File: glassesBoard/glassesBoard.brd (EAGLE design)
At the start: 87.4 x 30.9 mm, 131 parts, among them J1 BM10NB(0.8)-16DS-0.4V(51), J2 DF30FC-30DS-0.4V, J3 S2B-XH-A(LF)(SN), J4 GRPB042MWCN-RC, J5 0787324001, J6 FH26W-39S-0.3SHW, J7 105450-0101, U10 ATTINY20-MMH, U11 SN65LVDS822VQFN48, U12 NLAS2750, U13 NX3020NAK, U14 SSM3J338RSOT-23F, U15 NX3020NAK, U16 SSM3J338RSOT-23F, U17 NX3020NAK, U18 2.8, U19 TCR2EF15SOT-25, U2 TPS613222A, U20 MICROSD, U21 MCP73833, U22 FXMA2104UMX, U23 NX3020NAK, U24 FXMA2104UMX, U25 FXMA2104UMX, U26 LM2665M6XSOT23-6, U3 1.8, U4 3.3, U5 SSM3J338RSOT-23F, U6 SSM3J338RSOT-23F, U7 SN65DSI83-Q1S-PQFP-G64, U8 IQS263BDFN10, U9 NX3020NAK

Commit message: more progress on routing
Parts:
- removed C30: 1uF, thanics-capacitor:C0402
- added R50: 10k, thanics-resistor:R0402
- moved R31 53.0 mm to (43.7, 27.6), turned to 90 degrees
- moved R30 47.6 mm to (42.5, 27.6), turned to 90 degrees
- moved R21 27.7 mm to (48.0, 21.2)
- moved R22 26.9 mm to (47.9, 19.1)
- moved C32 22.0 mm to (8.23, 14.3)
- moved C33 21.4 mm to (4.17, 14.5), turned to 90 degrees
- moved C29 9.30 mm to (6.15, 3.30)
- moved R49 8.11 mm to (7.57, 23.1), turned to 90 degrees
- moved R47 6.16 mm to (5.79, 24.2), turned to 180 degrees
- moved U25 5.41 mm to (5.84, 22.1), turned to 90 degrees
- moved C15 2.75 mm to (8.72, 19.8), flipped to the top, turned to 270 degrees
- moved C14 2.17 mm to (4.30, 19.1)
- moved C20 1.69 mm to (72.3, 22.3)
- moved J4 1.48 mm to (1.83, 24.7)
- moved J1 1.34 mm to (6.26, 18.5)
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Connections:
- removed net !SHUTDOWN_LVDS: U11.37
- removed net LED_B: J4.4, U$1.J2.2, U$1.J2.60
- removed net LED_G: J4.3, U$1.J2.58, U$1.J2.8
- removed net LED_R: J4.5, U$1.J2.6
- removed net SCL: J6.8
- removed net SDA: J6.7
- net +1V5: no longer C30.1
- net +1V8: now also R50.2
- net DSI_EN: now also U$1.J1.76, U11.37; no longer U$1.J2.63
- net GND: no longer C30.2
- net I2C3_SCL: now also J6.8
- net I2C3_SDA: now also J6.7
- net RESETB: now also R50.1
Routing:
- net PM_RESIN_N: track 0.00 -> 70.8 mm, vias 0 -> 3
- net I2C2_SDA: track 0.00 -> 68.6 mm, vias 0 -> 3
- net CAM1_RST: track 0.00 -> 68.3 mm, vias 0 -> 1
- net I2C2_SCL: track 0.00 -> 67.4 mm, vias 0 -> 3
- net BOOT_CONFIG_1: track 0.00 -> 65.0 mm, vias 0 -> 1
- net +1V8: track 17.6 -> 81.1 mm, vias 18 -> 31
- net GND: track 17.5 -> 80.6 mm, vias 15 -> 44
- net CAM1_XCLK: track 0.00 -> 61.3 mm, vias 0 -> 1
- net P$1: track 54.5 -> 114.7 mm, vias 2 -> 8
- net DSI_EN: track 0.00 -> 59.2 mm, vias 0 -> 2
- net +5V: track 55.0 -> 112.9 mm, vias 8 -> 11
- net VREG_L11_SDC: track 0.00 -> 56.7 mm, vias 0 -> 4
- net PHONE_ON_N: track 0.00 -> 55.7 mm, vias 0 -> 2
- net CAM1_PWDN: track 0.00 -> 48.7 mm, vias 0 -> 1
- net FORCED_USB_BOOT: track 0.00 -> 47.2 mm, vias 0 -> 3
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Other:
- board size 87.4 x 30.9 mm -> 87.4 x 31.9 mm

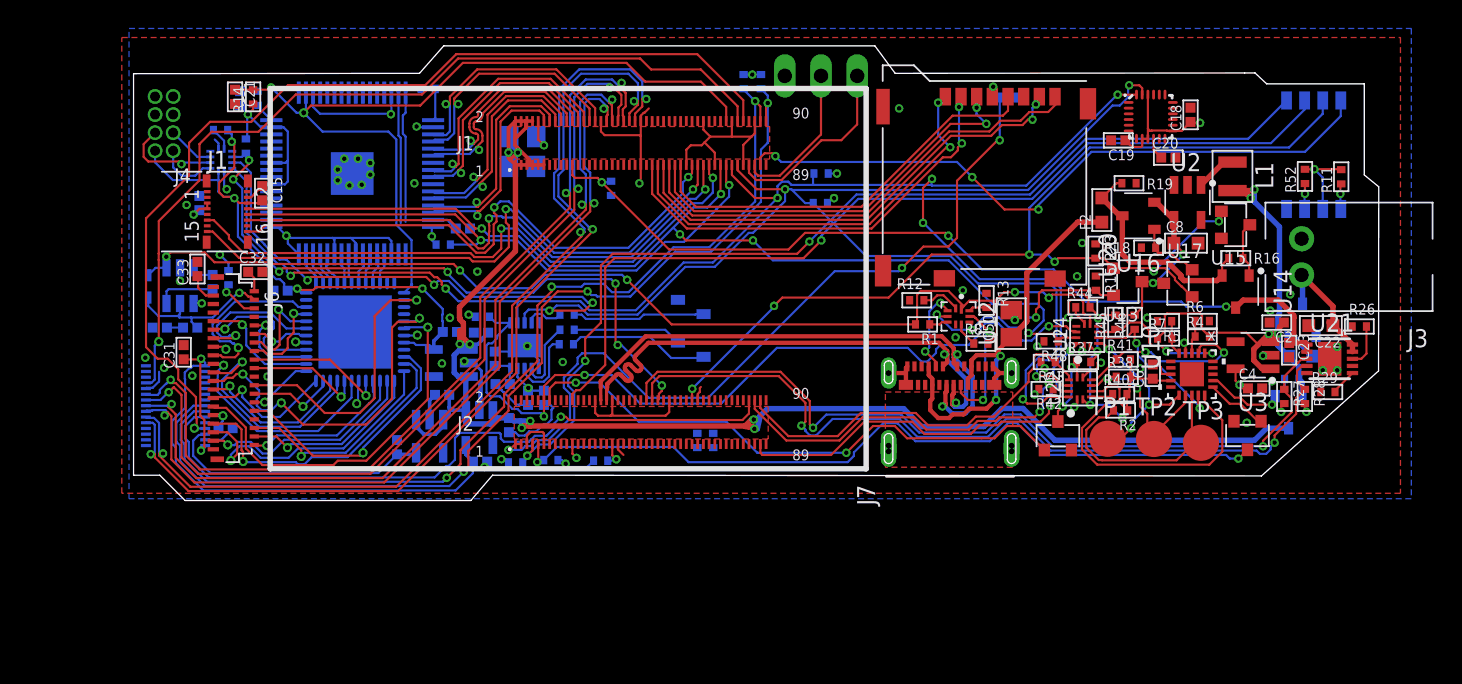
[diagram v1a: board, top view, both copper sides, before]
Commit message: made more progress on routing, and added capacitive touch slider board
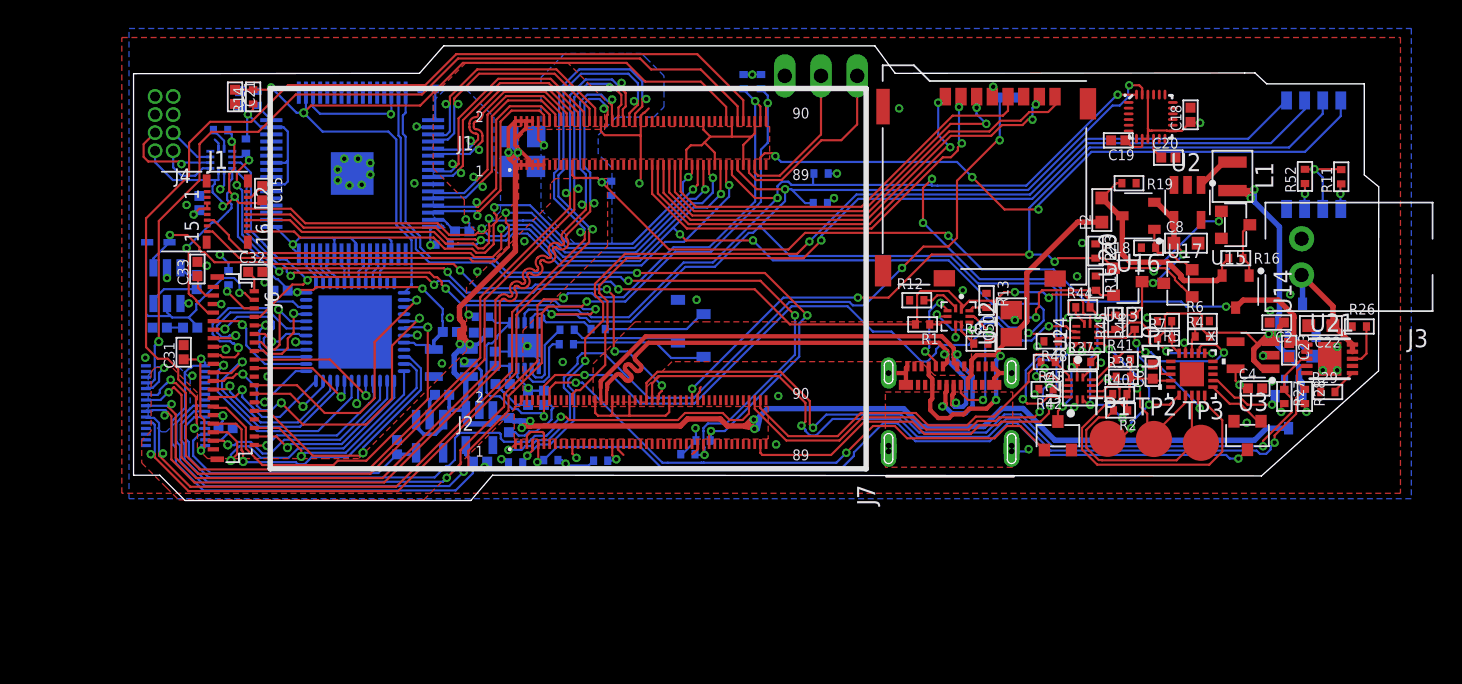
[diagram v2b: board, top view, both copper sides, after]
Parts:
- moved D1 3.18 mm to (1.42, 16.4), turned to 180 degrees
- moved R36 2.41 mm to (32.3, 10.3)
- moved R33 1.17 mm to (38.6, 1.47), turned to 0 degrees
- moved C34 1.12 mm to (4.11, 13.6)
- moved U26 0.91 mm to (2.03, 13.3)
- moved R32 0.71 mm to (39.7, 2.44), turned to 0 degrees
- moved C17 0.21 mm to (22.8, 17.1)
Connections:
- net I2C0_SCL: now also J6.8
- net I2C0_SDA: now also J6.7
- net I2C3_SCL: no longer J6.8
- net I2C3_SDA: no longer J6.7
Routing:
- net I2C3_SCL: track 9.22 -> 54.8 mm, vias 0 -> 3
- net I2C3_SDA: track 9.23 -> 53.7 mm, vias 0 -> 3
- net I2C0_SDA: track 109.5 -> 122.6 mm, vias 7 -> 8
- net I2C0_SCL: track 126.7 -> 135.0 mm
- net GND: track 80.6 -> 86.9 mm, vias 44 -> 53
- net +10V: track 11.2 -> 17.1 mm
- net N$30: track 2.68 -> 5.25 mm
- net MIPI_CSI1_CLK_P: track 58.6 -> 61.2 mm
- net MIPI_CSI1_CLK_N: track 58.1 -> 60.6 mm
- net !TOUCH_INT_1V8: track 57.3 -> 59.8 mm
- net +1V8: track 81.1 -> 83.5 mm, vias 31 -> 32
- net RX3: track 9.35 -> 7.34 mm
- net DE: track 19.8 -> 18.7 mm
- net !GESTURE_INT: track 46.1 -> 45.1 mm
- net CLKX: track 24.6 -> 23.7 mm
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
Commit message: about to move fingerprint sensor connector and add backlight connector
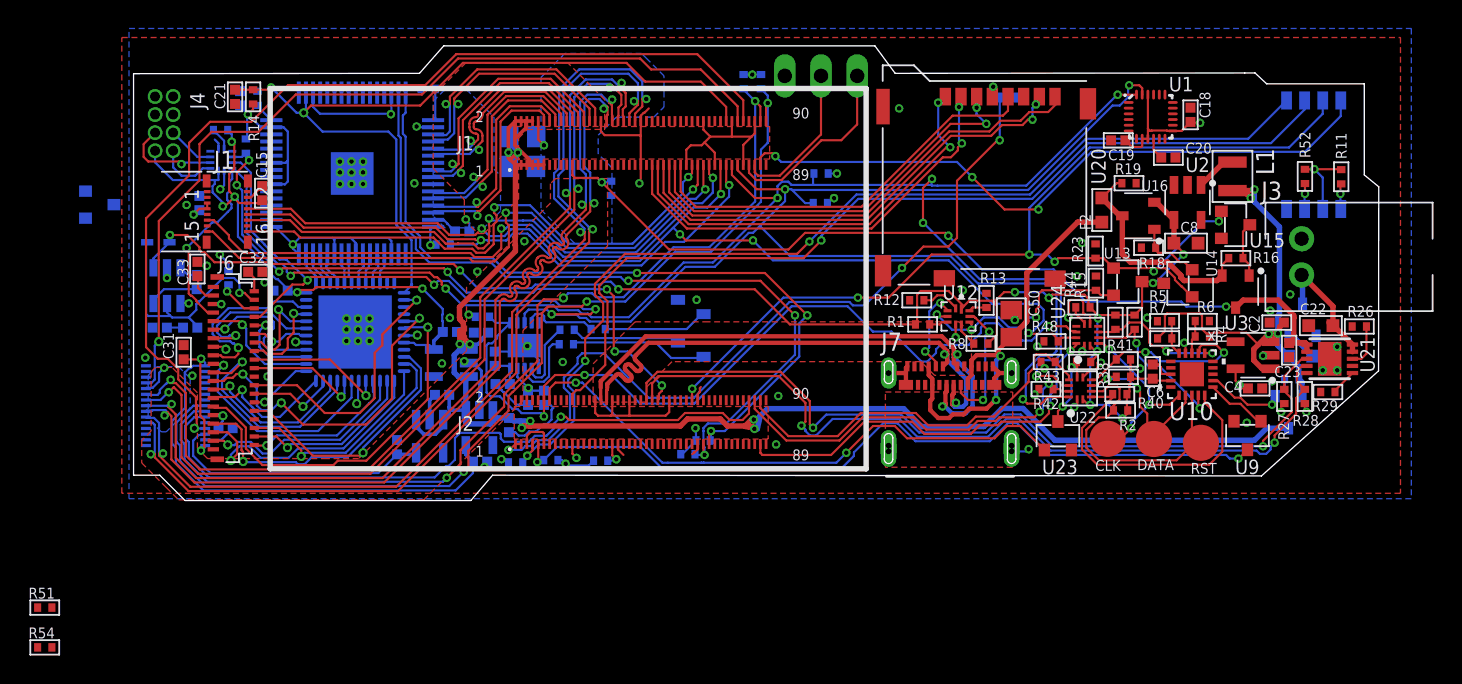
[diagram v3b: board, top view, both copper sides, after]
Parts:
- added R51: 8R, thanics-resistor:R0402
- added R54: 10k, thanics-resistor:R0402
- added U27: NX3020NAK, glasses:SOT-23_(TO-236AB)
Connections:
- new net BACKLIGHT_PWM: R54.2, U$1.J2.6, U27.G
- new net N$41: R51.1, U27.D
- net GND: now also R54.1, U27.S
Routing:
- net +5V: track 113.5 -> 112.9 mm
- net GND: vias 53 -> 63
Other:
- board text added: "CLK"
- board text added: "DATA"
- board text added: "FASTBOOT"
- board text added: "RST"
- board text added: "SD BOOT"
- board text added: "USB BOOT"
- board text added: "USB DEVICE"

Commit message: finished rev 1 of design
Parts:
- added J8: 5-520315-2, thanics-connector:5-520315-2
- moved R51 29.7 mm to (3.51, 18.6), flipped to the bottom, turned to 180 degrees
- moved R54 28.9 mm to (0.10, 16.0), flipped to the bottom
- moved C16 13.1 mm to (20.2, 27.2), turned to 180 degrees
- moved C14 7.75 mm to (4.91, 26.8)
- moved J1 5.69 mm to (5.66, 24.2), turned to 180 degrees
- moved C15 3.74 mm to (5.34, 21.4), turned to 0 degrees
- moved D1 3.58 mm to (-0.46, 13.3), turned to 90 degrees
- moved U27 3.35 mm to (0.56, 18.2)
- moved R53 1.88 mm to (22.3, 27.2), turned to 0 degrees
- moved R25 1.63 mm to (7.37, 25.2), turned to 180 degrees
- moved C21 1.41 mm to (8.18, 26.9), flipped to the bottom
- moved R14 1.31 mm to (6.81, 26.9), flipped to the bottom
- moved C19 1.23 mm to (69.6, 22.5)
- moved J4 1.17 mm to (0.66, 24.8)
- moved R47 0.61 mm to (5.18, 24.2), turned to 0 degrees
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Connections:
- new net N$43: J8.2, R51.2
- net +3V3: now also J8.1
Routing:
- net BACKLIGHT_PWM: track 0.00 -> 47.7 mm, vias 0 -> 3
- net +3V3: track 43.2 -> 57.8 mm
- net SPI0_CLK: track 39.1 -> 46.9 mm
- net +1V8: track 83.5 -> 90.3 mm, vias 32 -> 31
- net SPI0_CS: track 39.5 -> 45.9 mm
- net !FINGER_INT_1V8: track 74.0 -> 79.3 mm
- net !FINGER_RST: track 42.3 -> 47.0 mm
- net SPI0_MOSI: track 42.7 -> 46.7 mm
- net GND: track 86.9 -> 83.4 mm, vias 63 -> 66
- net +10V: track 17.1 -> 13.7 mm
- net CAM1_XCLK: track 61.3 -> 63.9 mm
- net CAM1_RST: track 68.3 -> 70.9 mm
- net N$43: track 0.00 -> 2.43 mm
- net I2C0_SCL_3V3: track 6.97 -> 9.04 mm, vias 1 -> 2
- net SPI0_MISO: track 43.3 -> 45.0 mm
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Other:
- board size 87.4 x 31.9 mm -> 88.7 x 31.9 mm
- board text added: "+-"

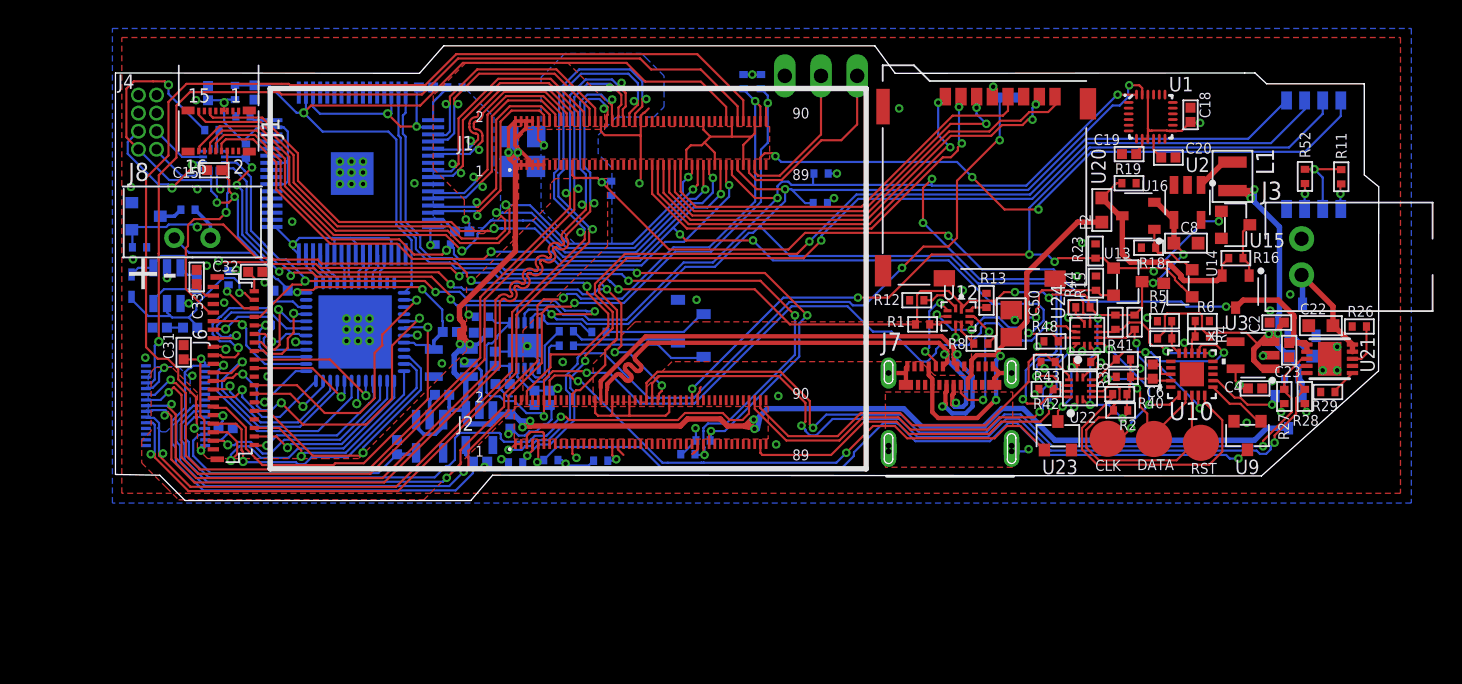
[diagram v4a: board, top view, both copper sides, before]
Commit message: Fixed backwards display connector and changed backlight connector
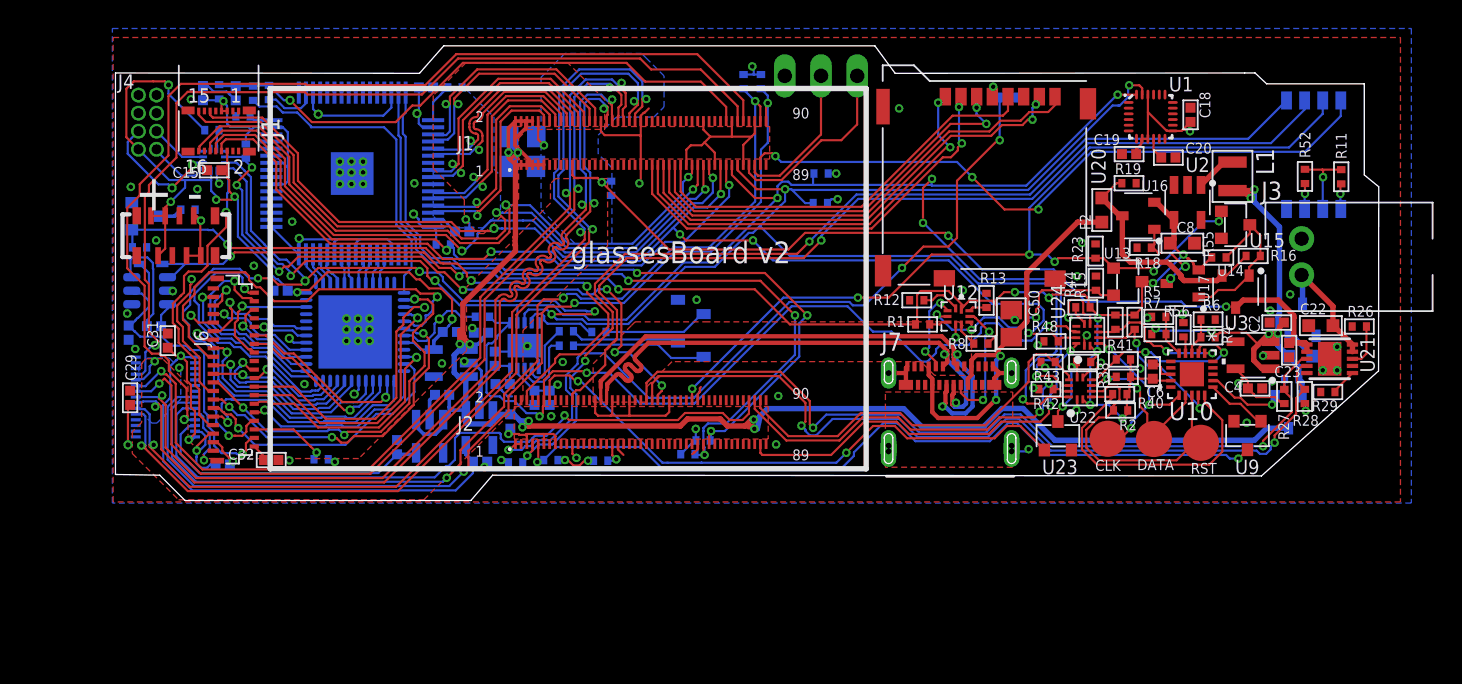
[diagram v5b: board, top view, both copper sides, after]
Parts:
- removed C36: 1uF, thanics-capacitor:C0402
- added R55, R56: 10k, thanics-resistor:R0402
- added R57, R58: 0R, thanics-resistor:R0402
- J8: value 5-520315-2 -> 62674-081121ALF; device thanics-connector:5-520315-2 -> thanics-connector:62674-081121ALF
- U17: value NX3020NAK -> SSM3J338RSOT-23F; device glasses:SOT-23_(TO-236AB) -> glasses:SOTFL95P240X80-3
- moved R50 14.3 mm to (12.9, 1.12), turned to 180 degrees
- moved C33 13.3 mm to (5.94, 0.76), flipped to the bottom, turned to 0 degrees
- moved C32 13.3 mm to (9.35, 1.07)
- moved C29 7.04 mm to (-0.56, 5.44), flipped to the top, turned to 90 degrees
- moved C35 4.33 mm to (-0.66, 10.0), turned to 270 degrees
- moved C34 4.31 mm to (1.12, 10.5), turned to 180 degrees
- moved D1 2.05 mm to (0.91, 14.8), turned to 180 degrees
- moved C31 1.38 mm to (2.08, 9.45)
- moved C21 1.32 mm to (6.86, 26.8)
- moved U26 1.27 mm to (0.81, 13.0), turned to 0 degrees
- moved R16 1.23 mm to (78.3, 15.4)
- moved R14 1.12 mm to (5.69, 26.9)
- moved J2 0.94 mm to (1.92, 5.49)
- moved R7 0.51 mm to (71.7, 9.91)
- moved R5 0.51 mm to (71.7, 11.1)
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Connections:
- new net N$45: R56.1, U10.4
- new net USB_POW: R16.1, R55.1, U14.1, U15.D, U17.1
- net +10V: now also J6.36; no longer J6.4
- net +1V8: now also J6.25, J6.9, R56.2; no longer J6.15, J6.31, U10.4
- net +3V3: now also J8.2, J8.3
- net +5V: now also R55.2, U17.2; no longer U17.D
- net B0: now also J6.2, U11.11; no longer J6.38, U11.4
- net B1: now also J6.3, U11.12; no longer J6.37, U11.3
- net B2: now also J6.4, U11.13; no longer J6.36, U11.2
- net B3: now also J6.5, U11.14; no longer J6.35, U11.1
- net B4: now also J6.6, U11.15; no longer J6.34, U11.48
- net B5: now also J6.7, U11.16; no longer J6.33, U11.47
- net B6: now also J6.10, U11.18; no longer J6.30, U11.46
- net B7: now also J6.11, U11.19; no longer J6.29, U11.42
- net CABC: now also J6.8; no longer J6.32
- net CLKX: now also J6.17; no longer J6.23
- net COM: now also J6.38; no longer J6.2
- net CSTN: now also J6.37; no longer J6.3
- net DE: now also J6.16, U11.22; no longer J6.24, U11.38
- net DSI_EN: now also R57.1, R58.1; no longer U11.37, U7.2
- net G0: now also J6.12, U11.2; no longer J6.28, U11.13
- net G1: now also J6.13, U11.3; no longer J6.27, U11.12
- net G2: now also J6.14, U11.4; no longer J6.26, U11.11
- net G3: now also J6.15, U11.5; no longer J6.25, U11.10
- net G4: now also J6.19, U11.7; no longer J6.21, U11.9
- net G6: now also J6.21, U11.9; no longer J6.19, U11.7
- net G7: now also J6.22, U11.10; no longer J6.18, U11.5
- net GND: now also C35.2, J6.18, J6.35; no longer C36.2, J6.22, J6.5
- net I2C0_SCL: now also J6.32; no longer J6.8
- net I2C0_SDA: now also J6.33; no longer J6.7
- net N$23: now also R57.2, U7.2; no longer R16.1, U14.1, U15.D
- net N$25: now also U17.3; no longer U17.S
- net N$42: now also R58.2, U11.37; no longer C35.2, C36.1
- net N$43: now also J8.6, J8.7, J8.8; no longer J8.2
- net R0: now also J6.23, U11.38; no longer J6.17, U11.22
- net R1: now also J6.24, U11.39; no longer J6.16, U11.21
- net R2: now also J6.26, U11.40; no longer J6.14, U11.20
- net R3: now also J6.27, U11.42; no longer J6.13, U11.19
- net R4: now also J6.28, U11.46; no longer J6.12, U11.18
- net R5: now also J6.29, U11.47; no longer J6.11, U11.16
- net R6: now also J6.30, U11.48; no longer J6.10, U11.15
- net R7: now also J6.31, U11.1; no longer J6.9, U11.14
- net RESETB: now also J6.34; no longer J6.6
- net TEST_HV: now also J6.39; no longer J6.1
- net USB_HS_ID: no longer U17.G
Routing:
- net N$42: track 1.13 -> 22.7 mm
- net +1V8: track 90.3 -> 111.5 mm, vias 31 -> 32
- net I2C0_SCL: track 134.9 -> 155.0 mm, vias 7 -> 9
- net DSI_EN: track 59.2 -> 40.8 mm
- net B7: track 26.3 -> 9.24 mm
- net R1: track 6.13 -> 20.6 mm
- net B6: track 18.2 -> 3.90 mm
- net R0: track 12.6 -> 26.9 mm, vias 1 -> 3
- net B5: track 21.2 -> 7.84 mm
- net R3: track 10.8 -> 23.6 mm, vias 1 -> 3
- net R4: track 4.16 -> 16.5 mm
- net R2: track 6.94 -> 19.1 mm
- net USB_POW: track 0.00 -> 11.3 mm
- net DE: track 18.7 -> 8.68 mm
- net +10V: track 13.7 -> 23.6 mm
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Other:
- board text added: "+ -"
- board text added: "glassesBoard v2"
- board text removed: "+-"
